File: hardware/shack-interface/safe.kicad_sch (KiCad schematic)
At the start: 19 parts, among them U10 74LVC1G14, U11 74LVC1G02, U6 TPS3823A-33, U7 74LVC1G14, U8 74LVC1G08, U9 74LVC1G74

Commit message: Pre-order review; RF board seat keep-outs; part reuse P-1 to P-5
- docs/reviews/2026-10-31-pre-order-review.md: review of all three boards
  before ordering (verify scripts, ERC/DRC, pin maps, BOM, fab and case,
  firmware against spec, open items, part reuse).
- RF board (D-189, M-107): no other-net copper or vias under the case
  seats at S1 to S6 and the SO-239/SMA GND bosses; relay NC pads (pad 12)
  in netclass RF. Re-routed, DRC 0.
- Part reuse (D-190, M-108): one value text for 2k2, 100n 50V X7R and
  10n 50V X7R; shack PC817X order code as the controller; shack U4/U9 in
  VSSOP-8 (TI DCU, Nexperia DC) with fixed fan-out, re-routed.
  Netlists rf15, ctl15, si17; ERC 0.

Co-Authored-By: Claude Opus 5.5 <noreply@anthropic.com>
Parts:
- C71: value 100n -> 100n 50V X7R
- U9: footprint Package_SO:SSOP-8_2.95x2.8mm_P0.65mm -> Package_SO:VSSOP-8_2.3x2mm_P0.5mm; MPN SN74LVC1G74DCTR -> SN74LVC1G74DCUR
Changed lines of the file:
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@@
 			)
 		)
-		(property "Footprint" "Package_SO:SSOP-8_2.95x2.8mm_P0.65mm"
+		(property "Footprint" "Package_SO:VSSOP-8_2.3x2mm_P0.5mm"
 			(at 132.08 81.28 0)
 			(hide yes)
@@
 			)
 		)
-		(property "MPN" "SN74LVC1G74DCTR"
+		(property "MPN" "SN74LVC1G74DCUR"
 			(at 132.08 81.28 0)
 			(hide yes)
@@
 			)
 		)
-		(property "Value" "100n"
+		(property "Value" "100n 50V X7R"
 			(at 157.73 119.38 0)
 			(show_name no)

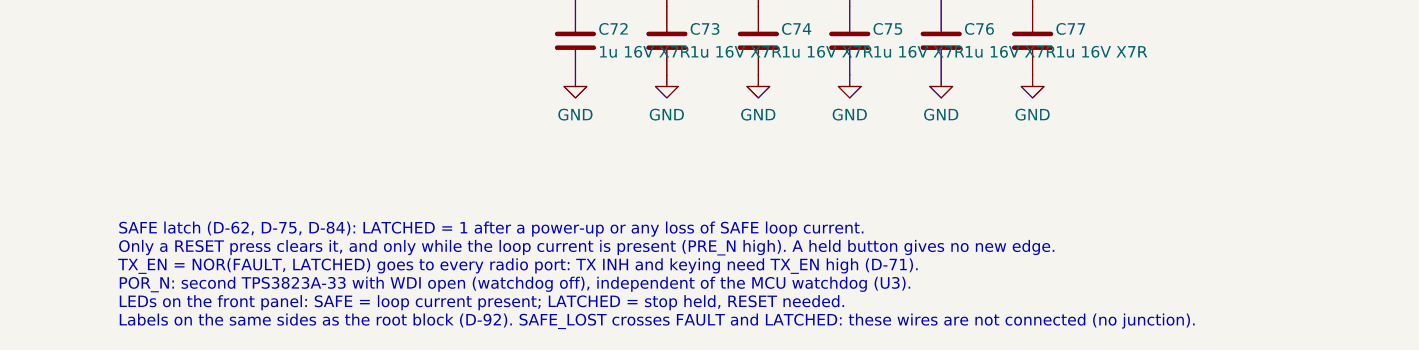
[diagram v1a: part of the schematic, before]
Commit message: S-10: MAX823SEUK+T first source, IRFL9014TRPBF-BE3 (D-195, M-118)
Supervisor U12 (controller), U3 and U6 (shack): MAX823SEUK+T first,
TPS3823A-33DBVR and APX823-29W5G-7 second. Same pin-out; RESET_N loads
are CMOS inputs; WDI and MR behave as the TPS3823 in our circuits.
RF Q1012 to Q1042: IRFL9014TRPBF-BE3. TLP176AM in stock at Mouser.
SO-239 83-798 stays single source, order first. Values and boards
unchanged. ERC 0 on all three.

Co-Authored-By: Claude Opus 5.5 <noreply@anthropic.com>
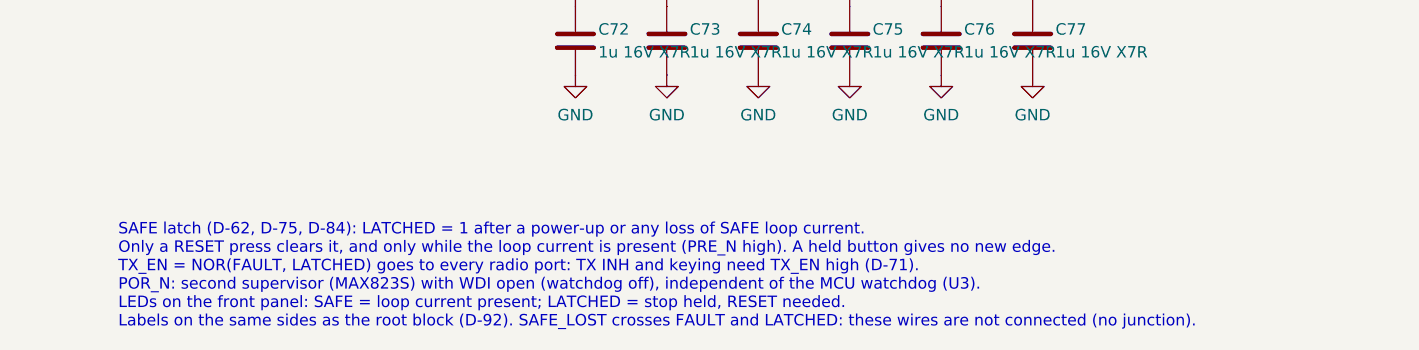
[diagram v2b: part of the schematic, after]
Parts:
- U6: MPN TPS3823A-33DBVR -> MAX823SEUK+T
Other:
- note added: "SAFE latch (D-62, D-75, D-84): LATCHED = 1 after a power-up or any loss of SAFE loop current. Only a RESET press clears it, and only while the loop current is present (PRE_N high). A held button gives no new edge. TX_EN = NOR(FAULT, LATCHED) goes to every radio port: TX INH and keying need TX_EN high (D-71). POR_N: second supervisor (MAX823S) with WDI open (watchdog off), independent of the MCU w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"
- note removed: "SAFE latch (D-62, D-75, D-84): LATCHED = 1 after a power-up or any loss of SAFE loop current. Only a RESET press clears it, and only while the loop current is present (PRE_N high). A held button gives no new edge. TX_EN = NOR(FAULT, LATCHED) goes to every radio port: TX INH and keying need TX_EN high (D-71). POR_N: second TPS3823A-33 with WDI open (watchdog off), independent of the MCU watchdog (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"
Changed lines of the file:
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@@
 			)
 		)
-		(property "Description" "Power-on and brown-out reset for the SAFE latch. WDI left open: watchdog disabled (TPS3823 7.3.4). MR open (90k pull-up)"
+		(property "Description" "Power-on and brown-out reset for the SAFE latch. WDI left open: watchdog disabled (MAX823 WDI pin; TPS3823 7.3.4). MR open (internal pull-up: MAX823 52k, TPS3823 90k). Second sources as U3 (D-195)"
 			(at 101.6 109.22 0)
 			(hide yes)
@@
 			)
 		)
-		(property "MPN" "TPS3823A-33DBVR"
+		(property "MPN" "MAX823SEUK+T"
 			(at 101.6 109.22 0)
 			(hide yes)
@@
 		)
 	)
-	(text "SAFE latch (D-62, D-75, D-84): LATCHED = 1 after a power-up or any loss of SAFE loop current.\nOnly a RESET press clears it, and only while the loop current is present (PRE_N high). A held button gives no new edge.\nTX_EN = NOR(FAULT, LATCHED) goes to every radio port: TX INH and keying need TX_EN high (D-71).\nPOR_N: second TPS3823A-33 with WDI open (watchdog off), independent of the MCU watchdog (U3).\nLEDs on the front panel: SAFE = loop current present; LATCHED = stop held, RESET needed.\nLabels on the same sides as the root block (D-92). SAFE_LOST crosses FAULT and LATCHED: these wires are not connected (no junction)."
+	(text "SAFE latch (D-62, D-75, D-84): LATCHED = 1 after a power-up or any loss of SAFE loop current.\nOnly a RESET press clears it, and only while the loop current is present (PRE_N high). A held button gives no new edge.\nTX_EN = NOR(FAULT, LATCHED) goes to every radio port: TX INH and keying need TX_EN high (D-71).\nPOR_N: second supervisor (MAX823S) with WDI open (watchdog off), independent of the MCU watchdog (U3).\nLEDs on the front panel: SAFE = loop current present; LATCHED = stop held, RESET needed.\nLabels on the same sides as the root block (D-92). SAFE_LOST crosses FAULT and LATCHED: these wires are not connected (no junction)."
 		(exclude_from_sim no)
 		(at 25.4 200.66 0)
